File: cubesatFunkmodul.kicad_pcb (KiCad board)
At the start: 4 copper layers, 85 x 85 mm, 102 parts, among them CON11 DISCO-CON1, CON21 DISCO-CON2, Q1 SSM3J334RLFTR-ND, Q2 AO3414, Q3 MMBT5551-TP, Q4 MMBT5551-TP, Q5 MMBT5551-TP, Q6 MMBT5551-TP, Q7 MMBT5551-TP, Q8 MMBT5551-TP, U1 MC74HC4538A, U2 MAX892, U3 ATMEGA128-16AU, U4 LTC3113, U5 RFM23BP, Y1 Crystal_GND24

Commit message: Adds new unit
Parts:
- added C21, C25: 10µF, Capacitors_SMD:C_1210_HandSoldering, F.Cu at (93.5, 129.1)
- added C22, C26, C27, C31, C32, C33, C40: 100nF, Capacitors_SMD:C_0603_HandSoldering, F.Cu at (93.5, 129.1)
- added C23: 1µF, Capacitors_SMD:C_1210_HandSoldering, F.Cu at (93.5, 129.1)
- added C24: 1nF, Capacitors_SMD:C_0603_HandSoldering, F.Cu at (93.5, 129.1)
- added C28, C29: 10pF, Capacitors_SMD:C_0603_HandSoldering, F.Cu at (93.5, 129.1)
- added C30: 10nF, Capacitors_SMD:C_0603_HandSoldering, F.Cu at (93.5, 129.1)
- added C34, C35, C36: 47µF, Capacitors_SMD:C_1210_HandSoldering, F.Cu at (93.5, 129.1)
- added C37: 47pF, Capacitors_SMD:C_0603_HandSoldering, F.Cu at (93.5, 129.1)
- added C38: 680pF, Capacitors_SMD:C_0603_HandSoldering, F.Cu at (93.5, 129.1)
- added C39: 12pF, Capacitors_SMD:C_0603_HandSoldering, F.Cu at (93.5, 129.1)
- added D19, D20, D21, D22, D23, D24, D25, D26, D27: TS4148C, Diodes_SMD:D_0603, F.Cu at (93.5, 129.1)
- added D28: DZ2J036M0LCT-ND, Diodes_SMD:D_SOD-323F, F.Cu at (93.5, 129.1)
- added L3: 10nH, Inductors_SMD:L_0603_HandSoldering, F.Cu at (93.5, 129.1)
- added L4: 5µH, Inductors_SMD:L_6.3x6.3_H3, F.Cu at (93.5, 129.1)
- added Q10: AO3414, TO_SOT_Packages_SMD:SOT-23, F.Cu at (93.5, 129.1)
- added Q11, Q12, Q13, Q14, Q15, Q16: MMBT5551-TP, TO_SOT_Packages_SMD:SOT-23, F.Cu at (93.5, 129.1)
- added Q9: SSM3J334RLFTR-ND, TO_SOT_Packages_SMD:SOT-23, F.Cu at (93.5, 129.1)
- added R46: 22k, Resistors_SMD:R_0603_HandSoldering, F.Cu at (93.5, 129.1)
- added R47, R48, R51, R52, R54, R56, R59, R60, R61, R62: 100k, Resistors_SMD:R_0603_HandSoldering, F.Cu at (93.5, 129.1)
- added R49: 47R, Resistors_SMD:R_0603_HandSoldering, F.Cu at (93.5, 129.1)
- added R50, R63: 100R, Resistors_SMD:R_0603_HandSoldering, F.Cu at (93.5, 129.1)
- added R53, R57, R58, R64, R65, R66, R67, R68, R69, R70, R78, R79, R80, R81, R82, R89, R90: 10k, Resistors_SMD:R_0603_HandSoldering, F.Cu at (93.5, 129.1)
- added R55: 15k, Resistors_SMD:R_0603_HandSoldering, F.Cu at (93.5, 129.1)
- added R71, R72, R73, R74, R75, R76, R77: 4k7, Resistors_SMD:R_0603_HandSoldering, F.Cu at (93.5, 129.1)
- added R83: 0R, Resistors_SMD:R_0603_HandSoldering, F.Cu at (93.5, 129.1)
- added R84: 90k9, Resistors_SMD:R_0603_HandSoldering, F.Cu at (93.5, 129.1)
- added R85: 49k9, Resistors_SMD:R_0603_HandSoldering, F.Cu at (93.5, 129.1)
- added R86: 6k81, Resistors_SMD:R_0603_HandSoldering, F.Cu at (93.5, 129.1)
- added R87: 121k, Resistors_SMD:R_0603_HandSoldering, F.Cu at (93.5, 129.1)
- added R88: 887k, Resistors_SMD:R_0603_HandSoldering, F.Cu at (93.5, 129.1)
- added REF**: MountingHole_3.2mm_M3, Mounting_Holes:MountingHole_3.2mm_M3, F.Cu at (55.5, 114.5)
- added REF**: MountingHole_3.2mm_M3, Mounting_Holes:MountingHole_3.2mm_M3, F.Cu at (131.5, 114.5)
- added REF**: MountingHole_3.2mm_M3, Mounting_Holes:MountingHole_3.2mm_M3, F.Cu at (131.5, 38.5)
- added U10: RFM23BP, HopeRF:RFM23BP, F.Cu at (102.9, 60.7)
- added U6: MC74HC4538A, Housings_SOIC:SOIC-16_3.9x9.9mm_Pitch1.27mm, F.Cu at (93.5, 129.1)
- added U7: MAX892, Maxim:µMAX-8, F.Cu at (93.5, 129.1)
- added U8: ATMEGA128-16AU, Housings_QFP:TQFP-64_14x14mm_Pitch0.8mm, F.Cu at (93.5, 129.1)
- added U9: LTC3113, Housings_SSOP:HTSSOP-20-1EP_4.4x6.5mm_Pitch0.65mm_ThermalPad, F.Cu at (93.5, 129.1)
- added Y2: Crystal_GND24, Crystals:Crystal_SMD_3225-4pin_3.2x2.5mm_HandSoldering, F.Cu at (93.5, 129.1)
- R11: moved to B.Cu
- moved D17 72.1 mm to (160.9, 111.2)
- moved D4 16.1 mm to (55.0, 99.2), turned to 0 degrees
- moved R11 12.3 mm to (53.4, 103.8), turned to 270 degrees
- moved R5 6.17 mm to (57.2, 95.7)
- moved R7 6.17 mm to (55.5, 95.7)
- moved U2 5.23 mm to (53.7, 104.2)
- moved D10 3.68 mm to (57.0, 106.7), turned to 0 degrees
- moved R10 3.59 mm to (53.6, 108.8), turned to 0 degrees
- moved C5 3.58 mm to (57.6, 109.8)
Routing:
- net /Funkmodul1/VCC: track 52.4 -> 142.4 mm, vias 12 -> 13
- net Net-(Q2-Pad2): track 7.79 -> 4.78 mm
- net /Funkmodul1/BURNWIRE: track 34.1 -> 31.5 mm
- net /Funkmodul1/~ON~: track 83.4 -> 85.1 mm
- net GND: track 58.3 -> 56.8 mm, vias 33 -> 35
- net /Connector/3.3V: track 104.8 -> 105.7 mm, vias 6 -> 7
- net Net-(R11-Pad2): track 4.03 -> 3.20 mm, vias 0 -> 1

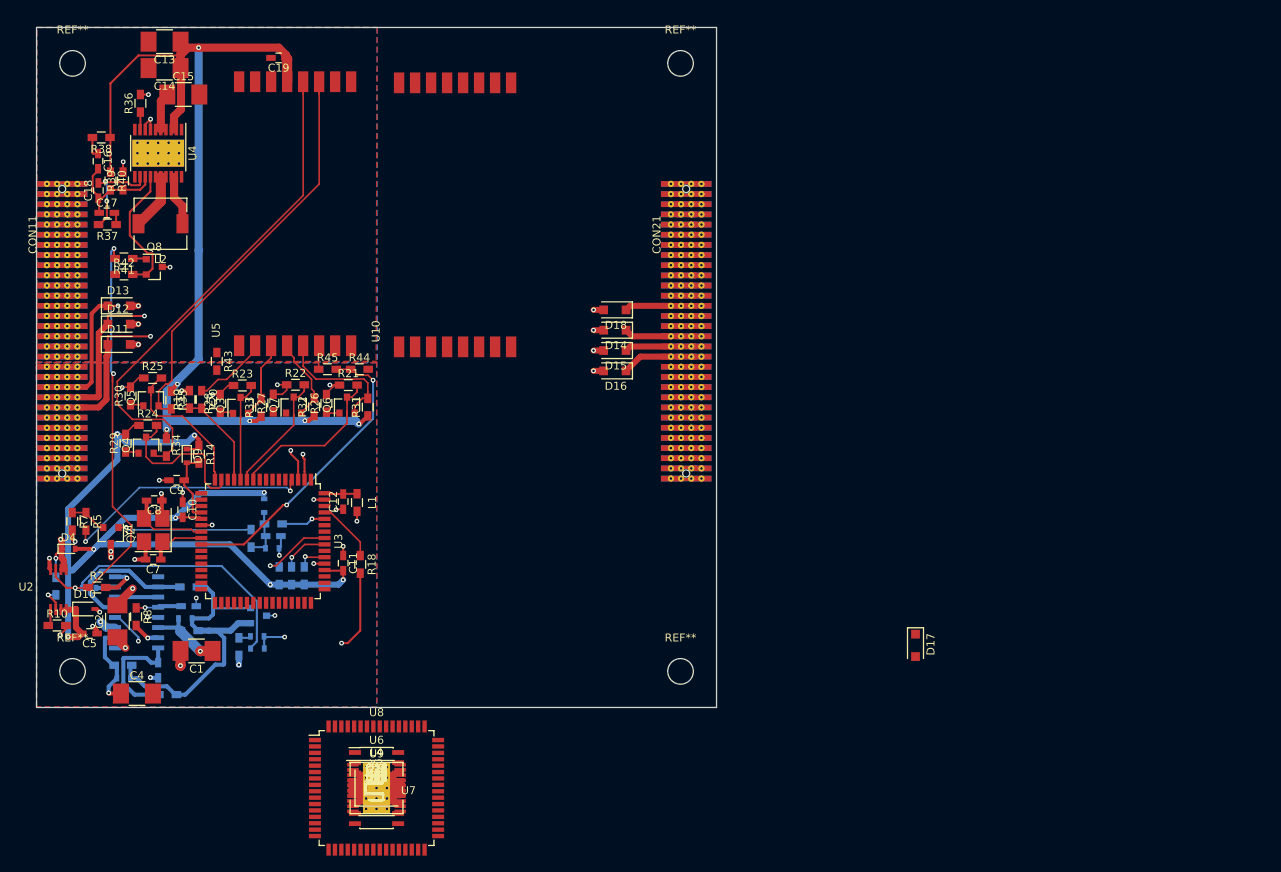
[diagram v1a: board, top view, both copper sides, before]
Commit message: Places µC of second module
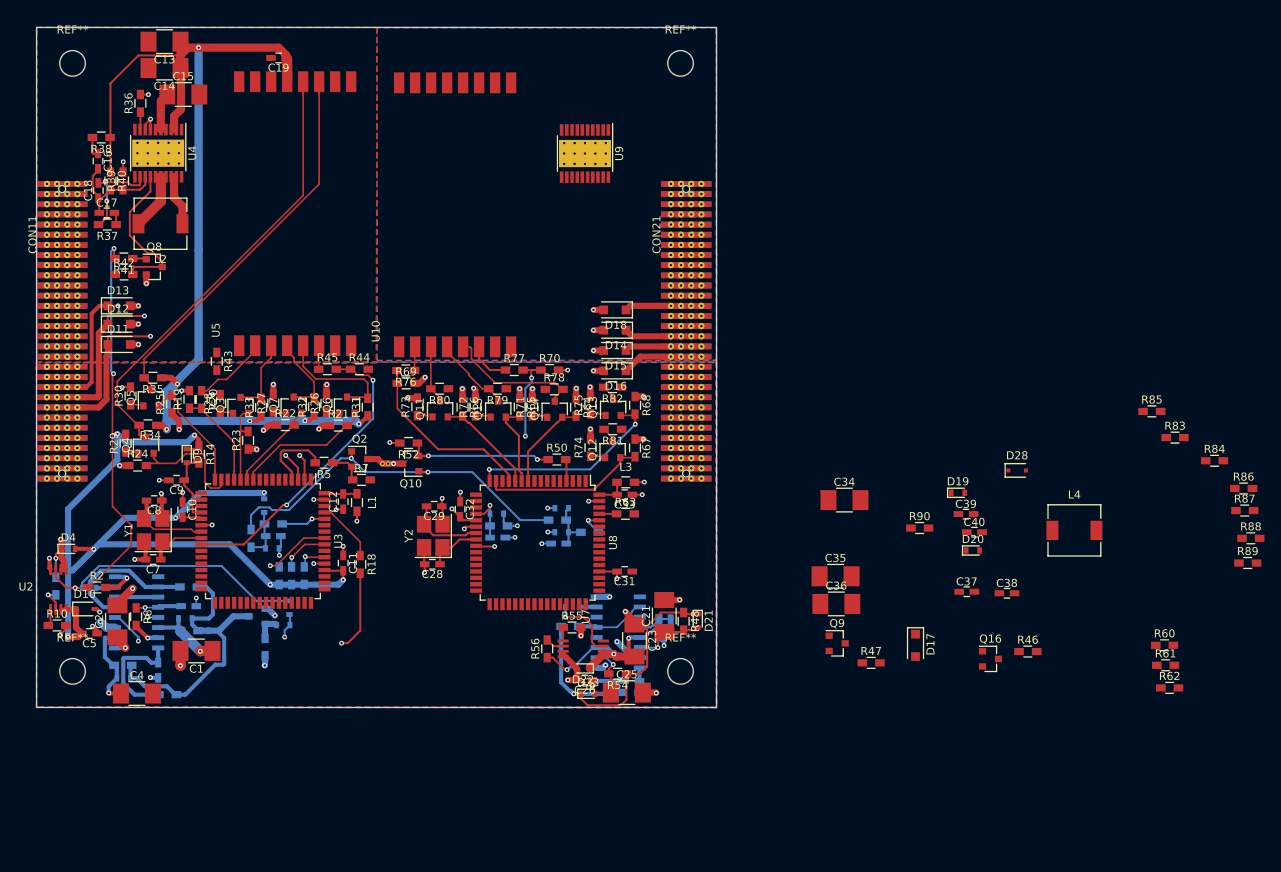
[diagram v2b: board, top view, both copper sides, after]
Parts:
- added REF**: VIA-0.6, connect-sm:VIA-0.6, F.Cu at (94.2, 88.5)
- added REF**: VIA-0.6, connect-sm:VIA-0.6, F.Cu at (95.0, 88.5)
- C22, C24, C27, C30, D24, D25, D26, D27, R49, R51, R53, R57, R58, R59, U6: moved to B.Cu
- moved R86 114.7 mm to (201.9, 91.6)
- moved R87 113.9 mm to (202.0, 94.4)
- moved R88 113.7 mm to (202.8, 97.9)
- moved R89 112.5 mm to (202.4, 100.9)
- moved R84 112.5 mm to (198.3, 88.2)
- moved R83 109.0 mm to (193.3, 85.3)
- moved R85 107.7 mm to (190.4, 82.0)
- moved R60 100.1 mm to (192.0, 111.2)
- moved R62 99.9 mm to (192.6, 116.5)
- moved R61 99.8 mm to (192.1, 113.7)
- moved L4 93.0 mm to (180.7, 96.9)
- moved D28 89.4 mm to (173.6, 89.4)
- moved U9 83.5 mm to (119.6, 49.8), turned to 270 degrees
- moved R46 83.2 mm to (174.9, 112.0)
- moved C38 82.5 mm to (172.3, 104.7)
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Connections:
- Q1 pad 1: Net-(D3-Pad1) -> /Connector/3.3V
- Q1 pad 3: /Connector/3.3V -> Net-(D3-Pad1)
- Q11 pad 2: /Funkmodul2/Funkeinheit2/MOSI_ -> /Funkmodul2/Funkeinheit2/MOSI
- Q11 pad 3: /Funkmodul2/Funkeinheit2/MOSI -> /Funkmodul2/Funkeinheit2/MOSI_
- Q12 pad 2: /Funkmodul2/Funkeinheit2/RXON_ -> /Funkmodul2/Funkeinheit2/RXON
- Q12 pad 3: /Funkmodul2/Funkeinheit2/RXON -> /Funkmodul2/Funkeinheit2/RXON_
- Q13 pad 2: /Funkmodul2/Funkeinheit2/TXON_ -> /Funkmodul2/Funkeinheit2/TXON
- Q13 pad 3: /Funkmodul2/Funkeinheit2/TXON -> /Funkmodul2/Funkeinheit2/TXON_
- Q14 pad 2: /Funkmodul2/Funkeinheit2/SS_ -> /Funkmodul2/Funkeinheit2/SS
- Q14 pad 3: /Funkmodul2/Funkeinheit2/SS -> /Funkmodul2/Funkeinheit2/SS_
- Q15 pad 2: /Funkmodul2/Funkeinheit2/SCK_ -> /Funkmodul2/Funkeinheit2/SCK
- Q15 pad 3: /Funkmodul2/Funkeinheit2/SCK -> /Funkmodul2/Funkeinheit2/SCK_
- Q16 pad 2: Net-(Q16-Pad2) -> GND
- Q16 pad 3: GND -> Net-(Q16-Pad3)
- Q3 pad 2: /Funkmodul1/Funkeinheit/MOSI_ -> /Funkmodul1/Funkeinheit/MOSI
- Q3 pad 3: /Funkmodul1/Funkeinheit/MOSI -> /Funkmodul1/Funkeinheit/MOSI_
- Q4 pad 2: /Funkmodul1/Funkeinheit/RXON_ -> /Funkmodul1/Funkeinheit/RXON
- Q4 pad 3: /Funkmodul1/Funkeinheit/RXON -> /Funkmodul1/Funkeinheit/RXON_
- Q5 pad 2: /Funkmodul1/Funkeinheit/TXON_ -> /Funkmodul1/Funkeinheit/TXON
- Q5 pad 3: /Funkmodul1/Funkeinheit/TXON -> /Funkmodul1/Funkeinheit/TXON_
- Q6 pad 2: /Funkmodul1/Funkeinheit/SS_ -> /Funkmodul1/Funkeinheit/SS
- Q6 pad 3: /Funkmodul1/Funkeinheit/SS -> /Funkmodul1/Funkeinheit/SS_
- Q7 pad 2: /Funkmodul1/Funkeinheit/SCK_ -> /Funkmodul1/Funkeinheit/SCK
- Q7 pad 3: /Funkmodul1/Funkeinheit/SCK -> /Funkmodul1/Funkeinheit/SCK_
- Q8 pad 2: Net-(Q8-Pad2) -> GND
- Q8 pad 3: GND -> Net-(Q8-Pad3)
- Q9 pad 1: Net-(D21-Pad1) -> /Funkmodul2/3.3V
- Q9 pad 3: /Funkmodul2/3.3V -> Net-(D21-Pad1)
- R42 pad 2: Net-(Q8-Pad2) -> Net-(Q8-Pad3)
- R90 pad 2: Net-(Q16-Pad2) -> Net-(Q16-Pad3)
- U4 pad 14: Net-(Q8-Pad2) -> Net-(Q8-Pad3)
- U9 pad 14: Net-(Q16-Pad2) -> Net-(Q16-Pad3)
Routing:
- net GND: track 56.8 -> 99.5 mm, vias 35 -> 54
- net Net-(D21-Pad1): track 0.00 -> 41.4 mm, vias 0 -> 1
- net WIRE_CONN: track 16.7 -> 47.5 mm, vias 1 -> 2
- net /Funkmodul2/VCC: track 0.00 -> 29.5 mm, vias 0 -> 16
- net /Funkmodul2/Funkeinheit2/NIRQ: track 0.00 -> 28.6 mm, vias 0 -> 3
- net /Funkmodul2/3.3V: track 0.00 -> 26.3 mm, vias 0 -> 3
- net /Funkmodul2/Funkeinheit2/TXON: track 0.00 -> 25.2 mm, vias 0 -> 2
- net /Funkmodul2/Funkeinheit2/MISO: track 0.00 -> 22.9 mm
- net /Funkmodul1/BURNWIRE: track 31.5 -> 9.65 mm, vias 2 -> 0
- net /Funkmodul2/Funkeinheit2/RXON: track 0.00 -> 20.5 mm
- net Net-(Q8-Pad3): track 0.00 -> 19.0 mm
- net Net-(Q10-Pad2): track 0.00 -> 18.1 mm, vias 0 -> 2
- net /Funkmodul2/Funkeinheit2/SS_: track 0.00 -> 17.4 mm
- net Net-(Q8-Pad2): track 16.8 -> 0.00 mm
- net /Funkmodul2/Funkeinheit2/MOSI: track 0.00 -> 12.9 mm
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- added copper zone on B.Cu, net /Funkmodul2/Funkeinheit2/PGND
- added copper zone on F.Cu, net /Funkmodul2/Funkeinheit2/PGND
- added copper zone on In2.Cu, net /Funkmodul2/VCC

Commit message: Places all Components of second module
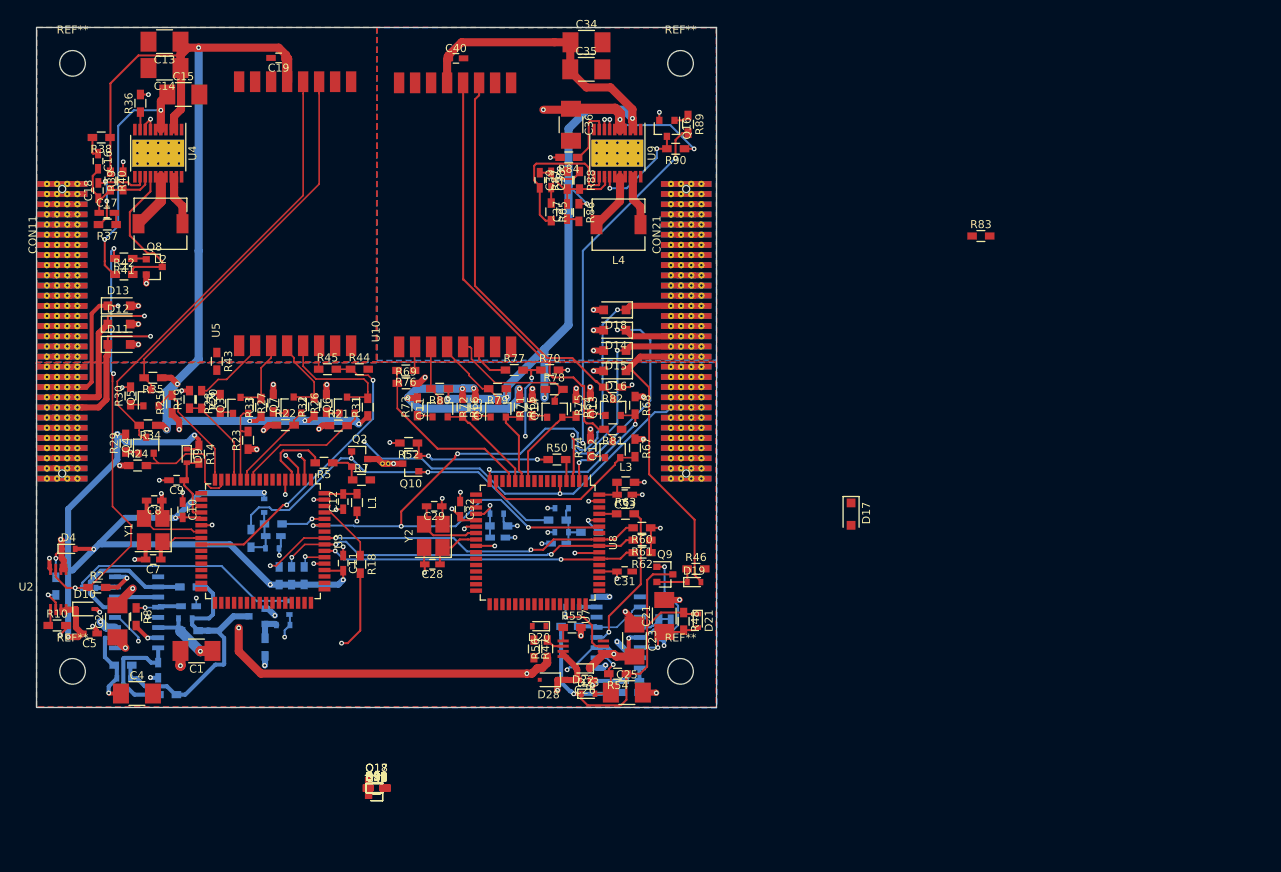
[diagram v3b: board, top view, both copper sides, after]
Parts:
- added C41, C42: 100nF, Capacitors_SMD:C_0603_HandSoldering, F.Cu at (93.5, 129.1)
- added D29, D30, D31, D32: TS4148C, Diodes_SMD:D_0603, F.Cu at (93.5, 129.1)
- added Q17, Q18: AO3414, TO_SOT_Packages_SMD:SOT-23, F.Cu at (93.5, 129.1)
- added R91, R95: 100R, Resistors_SMD:R_0603_HandSoldering, F.Cu at (93.5, 129.1)
- added R92, R96: 100k, Resistors_SMD:R_0603_HandSoldering, F.Cu at (93.5, 129.1)
- added R93, R94, R97, R98: 10k, Resistors_SMD:R_0603_HandSoldering, F.Cu at (93.5, 129.1)
- moved R88 95.1 mm to (118.9, 53.1), turned to 270 degrees
- moved R87 94.2 mm to (117.3, 53.1), turned to 90 degrees
- moved R86 90.0 mm to (118.8, 57.1), turned to 270 degrees
- moved R84 89.2 mm to (117.5, 50.2), turned to 180 degrees
- moved R89 88.9 mm to (132.4, 46.1), turned to 270 degrees
- moved C40 87.8 mm to (103.4, 37.9)
- moved R85 79.1 mm to (115.3, 57.1), turned to 270 degrees
- moved Q16 77.7 mm to (129.8, 46.6), turned to 270 degrees
- moved C38 76.9 mm to (115.3, 53.1), turned to 270 degrees
- moved C35 70.6 mm to (119.7, 39.2)
- moved C37 69.0 mm to (117.3, 57.0), turned to 90 degrees
- moved L4 68.6 mm to (123.7, 58.6), turned to 180 degrees
- moved C36 68.5 mm to (117.8, 46.2), turned to 270 degrees
- moved R62 68.1 mm to (126.7, 99.6), turned to 180 degrees
- moved C39 67.7 mm to (113.9, 53.1), turned to 270 degrees
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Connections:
- C23 pad 2: /Funkmodul2/3.3V -> /Connector/3.3V
- C24 pad 1: /Funkmodul2/3.3V -> /Connector/3.3V
- CON21 pad 16: /Connector/RX2 -> /Funkmodul2/RX
- CON21 pad 17: /Connector/TX2 -> /Funkmodul2/TX
- CON21 pad 6: /Connector/TDO-Rf -> /Funkmodul2/TDO
- D14 pad 1: /Connector/RX2 -> /Funkmodul2/RX
- D15 pad 1: /Connector/TX2 -> /Funkmodul2/TX
- D19 pad 2: /Funkmodul2/~MODULE_ON~ -> /Connector/~ENABLE2~
- D20 pad 2: /Funkmodul2/~MODULE_ON~ -> /Connector/~ENABLE2~
- D22 pad 1: /Funkmodul2/3.3V -> /Connector/3.3V
- Q9 pad 1: /Funkmodul2/3.3V -> /Connector/3.3V
- R56 pad 1: /Funkmodul2/3.3V -> /Connector/3.3V
- R60 pad 2: /Funkmodul2/TCK -> /Connector/TCK
- R61 pad 2: /Funkmodul2/TMS -> /Connector/TMS
- U3 pad 55: (no net) -> /Funkmodul2/TDI
- U3 pad 58: (no net) -> Net-(R94-Pad1)
- U6 pad 13: /Funkmodul2/3.3V -> /Connector/3.3V
- U6 pad 3: /Funkmodul2/3.3V -> /Connector/3.3V
- U7 pad 1: /Funkmodul2/3.3V -> /Connector/3.3V
- U7 pad 2: /Funkmodul2/3.3V -> /Connector/3.3V
- U8 pad 2: (no net) -> /Funkmodul2/RX
- U8 pad 3: (no net) -> /Funkmodul2/TX
- U8 pad 5: (no net) -> /Connector/~RBF~
- U8 pad 55: (no net) -> /Funkmodul2/TDO
- U8 pad 56: /Funkmodul2/TMS -> /Connector/TMS
- U8 pad 57: /Funkmodul2/TCK -> /Connector/TCK
- U8 pad 58: (no net) -> Net-(R98-Pad1)
- U8 pad 59: (no net) -> /Connector/BAT_OK
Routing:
- net /Funkmodul2/Funkeinheit2/5V: track 0.00 -> 122.9 mm, vias 0 -> 7
- net /Connector/TCK: track 9.40 -> 125.6 mm, vias 1 -> 3
- net /Connector/TMS: track 5.97 -> 117.5 mm, vias 1 -> 3
- net VBAT: track 6.02 -> 105.1 mm, vias 0 -> 5
- net /Connector/BAT_OK: track 5.82 -> 97.6 mm, vias 0 -> 5
- net /Connector/3.3V: track 106.3 -> 197.4 mm, vias 7 -> 13
- net /Funkmodul2/~ON~: track 8.75 -> 76.3 mm, vias 1 -> 3
- net /Funkmodul1/TDI: track 3.79 -> 70.5 mm
- net /Connector/~RBF~: track 0.00 -> 65.4 mm, vias 0 -> 3
- net /Funkmodul2/Funkeinheit2/RXON_: track 2.00 -> 55.3 mm
- net /Funkmodul2/TDO: track 0.00 -> 52.9 mm, vias 0 -> 1
- net /Funkmodul2/Funkeinheit2/TXON_: track 2.03 -> 48.9 mm
- net /Funkmodul2/VCC: track 29.5 -> 71.3 mm, vias 16 -> 17
- net /Funkmodul2/TDI: track 0.00 -> 39.4 mm, vias 0 -> 2
- net /Funkmodul2/RX: track 0.00 -> 33.7 mm, vias 0 -> 2
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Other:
- rule pad_to_mask_clearance: 0.2 -> 0.19
